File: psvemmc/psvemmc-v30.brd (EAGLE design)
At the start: 38 x 30.5 mm, 52 parts, among them J1 CON_HEADER_2X10-SHROUDED, J2 MF-CON-MICROUSB-RIGHT, U1 USB2244QFN, U2 LP3996_DSC_10, U3 TXS02612, U4 24AA00OT, U5 SN74AUP1G240DRY, U6 SN74AUP1G126DRY, U7 TPD4S014_DSQ_10, Y1 XRCGB

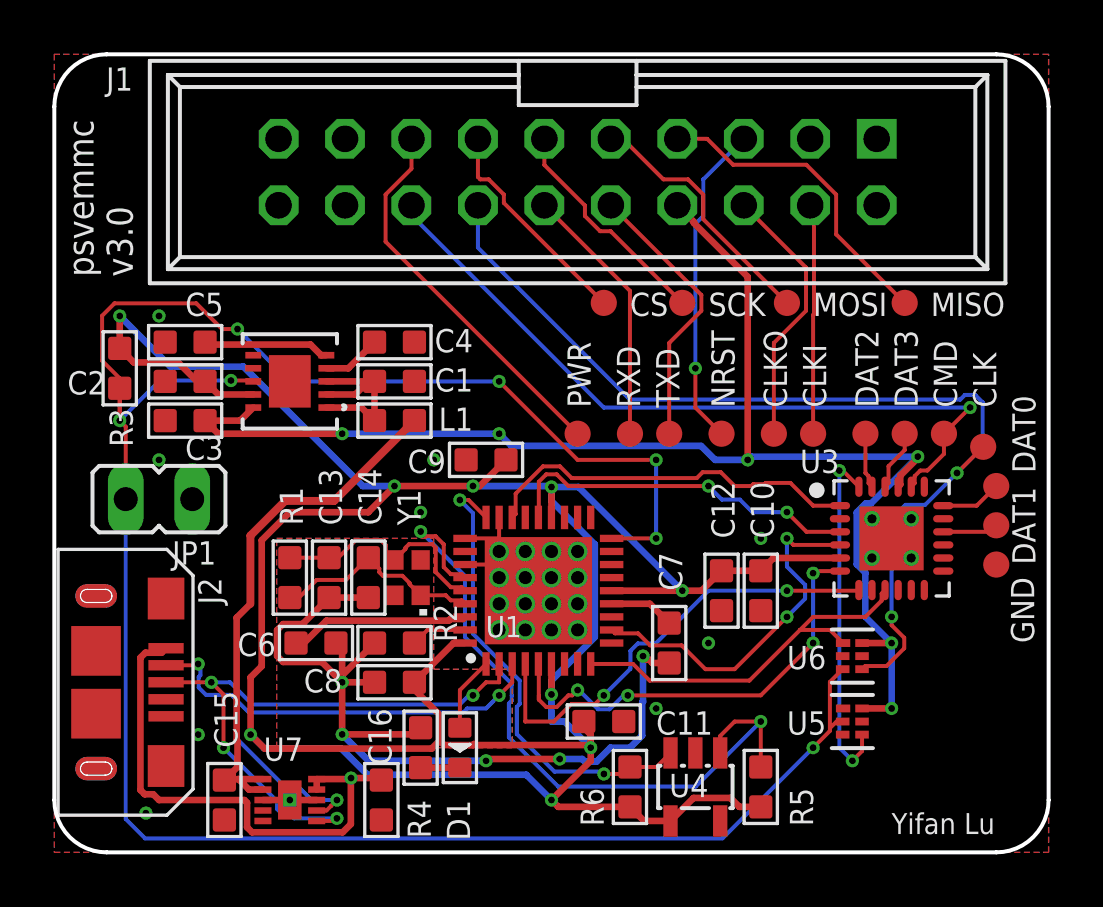
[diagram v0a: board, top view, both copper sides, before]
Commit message: psvemmc v3.1: fixed wrong pin ordering on clk buffer added pin 1 indicator to components missing them added title/value for sch in buffer components
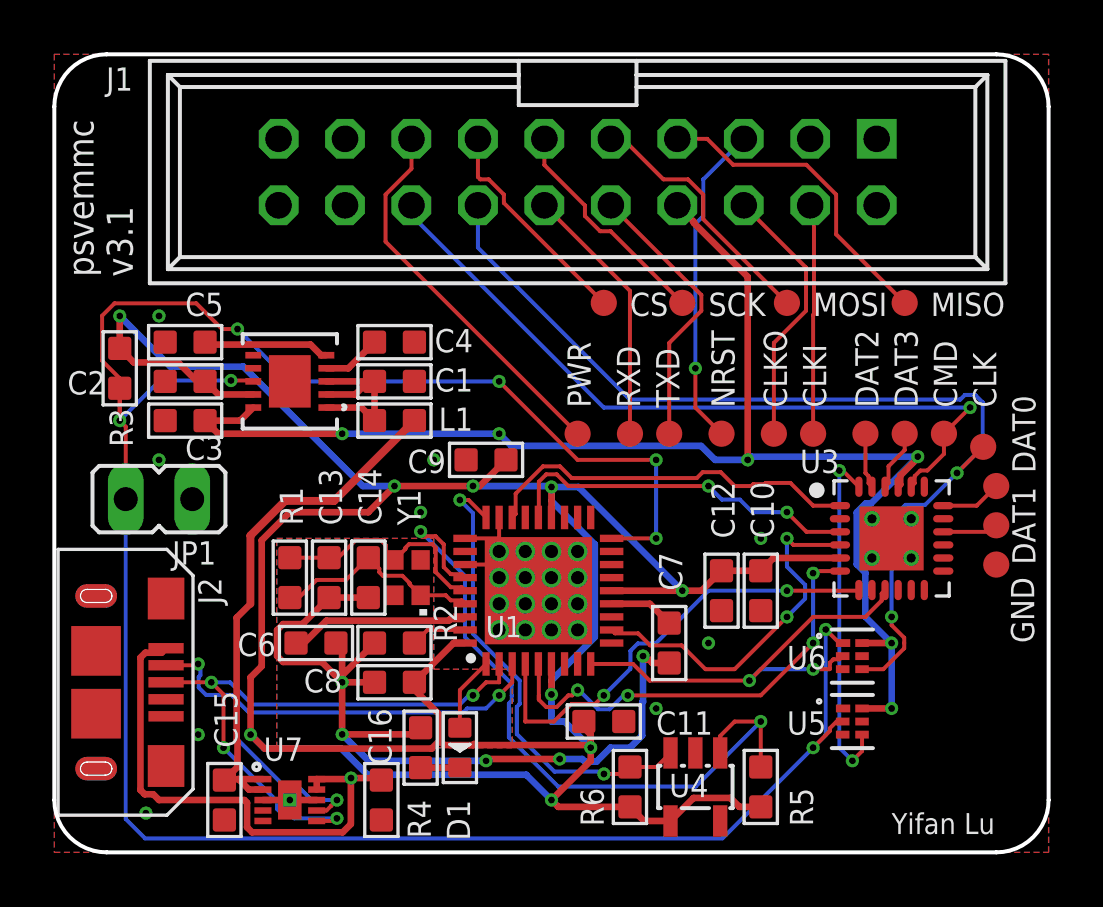
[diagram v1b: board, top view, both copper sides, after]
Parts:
- U5, U6: device SN74LVC1G125:DRY6 -> TI_Low_Power_Buffers:DRY6
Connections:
- net !USB_EN: now also U6.1; no longer U6.3
- net GND: now also U6.3; no longer U6.2
- net SD_CLK: now also U6.2; no longer U6.1
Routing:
- net !USB_EN: track 87.2 -> 90.4 mm, vias 7 -> 8
- net SD_CLK: track 15.0 -> 17.2 mm, vias 0 -> 2
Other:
- board text added: "psvemmc v3.1"
- board text removed: "psvemmc v3.0"
